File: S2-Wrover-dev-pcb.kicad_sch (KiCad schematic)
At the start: 23 parts, among them J1 USB_C_Receptacle_USB2.0, P1 CONN_02X13, P3 CONN_02X13, SW1 RESET, SW2 BOOT, U1 MCP1700-1202E_SOT23, U2 ESP32-S2-WROVER, U3 TPS2113APW, U4 TP4056

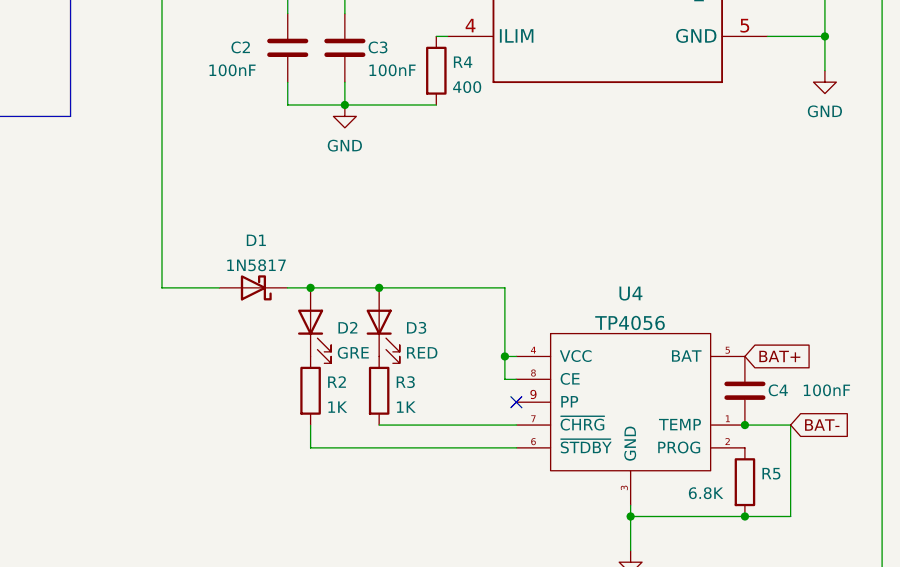
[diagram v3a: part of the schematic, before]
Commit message: Update schematic and assign footprints
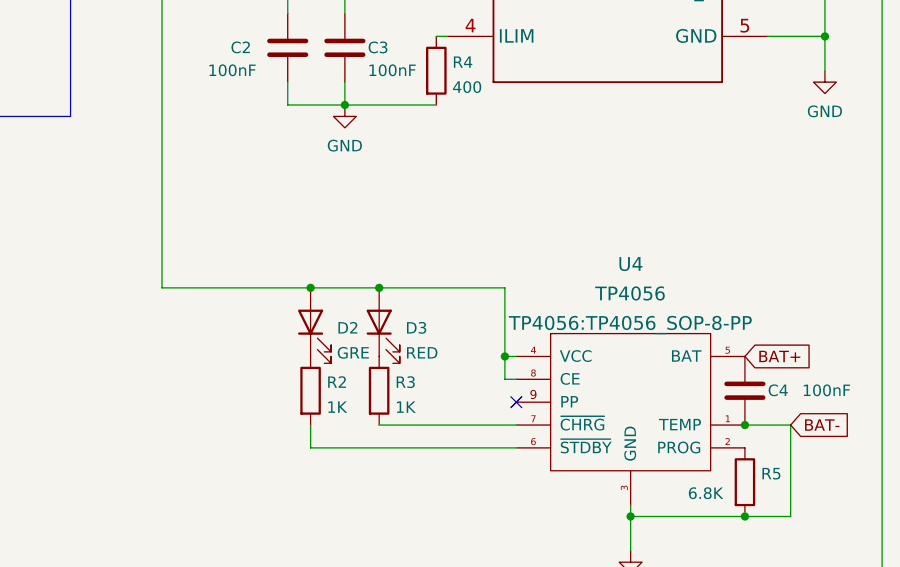
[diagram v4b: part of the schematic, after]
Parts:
- removed D1: 1N5817, Diode_SMD:D_SOD-123, symbol Device:D_Schottky
- P1, P3: footprint Pin_Headers:Pin_Header_Straight_2x13 -> Connector_PinHeader_2.54mm:PinHeader_2x13_P2.54mm_Vertical
- U3: footprint PW0008A_N -> footprint:TPS2113APW
- U4: footprint (none) -> TP4056:TP4056_SOP-8-PP
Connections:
- net VBUS: now also D2.2 (A), D3.2 (A), U4.4 (VCC), U4.8 (CE)
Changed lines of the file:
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@@
-    (stroke (width 0) (type default) (color 0 0 0 0))
-  )
-  (wire (pts (xy 213.36 86.36) (xy 215.9 86.36))
     (stroke (width 0) (type default) (color 0 0 0 0))
   )
@@
     (stroke (width 0) (type default) (color 0 0 0 0))
   )
-  (wire (pts (xy 199.39 86.36) (xy 205.74 86.36))
+  (wire (pts (xy 199.39 86.36) (xy 215.9 86.36))
     (stroke (width 0) (type default) (color 0 0 0 0))
   )
@@
     (property "Reference" "P1" (id 0) (at 125.73 146.05 0))
     (property "Value" "CONN_02X13" (id 1) (at 143.51 144.78 90))
-    (property "Footprint" "Pin_Headers:Pin_Header_Straight_2x13" (id 2) (at 172.72 146.05 0)
+    (property "Footprint" "Connector_PinHeader_2.54mm:PinHeader_2x13_P2.54mm_Vertical" (id 2) (at 172.72 146.05 0)
       (effects (font (size 1.27 1.27)) hide)
     )
@@
     (pin "9")
   )
-  (symbol (lib_id "Device:D_Schottky") (at 209.55 86.36 180) (unit 1)
-    (in_bom yes) (on_board yes) (fields_autoplaced)
-    (property "Reference" "D1" (id 0) (at 209.8675 81.1235 0))
-    (property "Value" "1N5817" (id 1) (at 209.8675 83.8986 0))
-    (property "Footprint" "Diode_SMD:D_SOD-123" (id 2) (at 209.55 86.36 0)
-      (effects (font (size 1.27 1.27)) hide)
-    )
-    (property "Datasheet" "~" (id 3) (at 209.55 86.36 0)
-      (effects (font (size 1.27 1.27)) hide)
-    )
-    (pin "1")
-    (pin "2")
-  )
   (symbol (lib_id "Device:LED") (at 223.52 90.17 90) (unit 1)
     (in_bom yes) (on_board yes) (fields_autoplaced)
@@
       (effects (font (size 1.524 1.524)))
     )
-    (property "Footprint" "PW0008A_N" (id 2) (at 248.92 52.324 0)
+    (property "Footprint" "footprint:TPS2113APW" (id 2) (at 248.92 52.324 0)
       (effects (font (size 1.524 1.524)) hide)
     )
@@
     (property "Reference" "P3" (id 0) (at 163.83 146.05 0))
     (property "Value" "CONN_02X13" (id 1) (at 181.61 144.78 90))
-    (property "Footprint" "Pin_Headers:Pin_Header_Straight_2x13" (id 2) (at 210.82 146.05 0)
+    (property "Footprint" "Connector_PinHeader_2.54mm:PinHeader_2x13_P2.54mm_Vertical" (id 2) (at 210.82 146.05 0)
       (effects (font (size 1.27 1.27)) hide)
     )
@@
   (symbol (lib_id "tp4056:TP4056") (at 251.46 100.33 0) (unit 1)
     (in_bom yes) (on_board yes) (fields_autoplaced)
-    (property "Reference" "U4" (id 0) (at 251.46 87.0361 0)
+    (property "Reference" "U4" (id 0) (at 251.46 83.7571 0)
       (effects (font (size 1.524 1.524)))
     )
-    (property "Value" "TP4056" (id 1) (at 251.46 90.3151 0)
+    (property "Value" "TP4056" (id 1) (at 251.46 87.0361 0)
       (effects (font (size 1.524 1.524)))
     )
-    (property "Footprint" "" (id 2) (at 251.46 100.33 0)
+    (property "Footprint" "TP4056:TP4056_SOP-8-PP" (id 2) (at 251.46 90.3151 0)
       (effects (font (size 1.524 1.524)))
     )
@@
       (reference "C4") (unit 1) (value "100nF") (footprint "Capacitor_SMD:C_0805_2012Metric")
     )
-    (path "/003cb78c-23ee-48ac-a35b-bde0860f178d"
-      (reference "D1") (unit 1) (value "1N5817") (footprint "Diode_SMD:D_SOD-123")
-    )
     (path "/e0ce6cb3-5c01-43ad-bab7-b796f3a1bb0f"
       (reference "D2") (unit 1) (value "GRE") (footprint "LED_SMD:LED_0805_2012Metric")
@@
     )
     (path "/00000000-0000-0000-0000-0000576c994f"
-      (reference "P1") (unit 1) (value "CONN_02X13") (footprint "Pin_Headers:Pin_Header_Straight_2x13")
+      (reference "P1") (unit 1) (value "CONN_02X13") (footprint "Connector_PinHeader_2.54mm:PinHeader_2x13_P2.54mm_Vertical")
     )
     (path "/9f932cfc-61d3-401a-b27a-c20d8327abe5"
-      (reference "P3") (unit 1) (value "CONN_02X13") (footprint "Pin_Headers:Pin_Header_Straight_2x13")
+      (reference "P3") (unit 1) (value "CONN_02X13") (footprint "Connector_PinHeader_2.54mm:PinHeader_2x13_P2.54mm_Vertical")
     )
     (path "/f7800b4d-8808-4d30-ba28-e36e5c5b35dc"
@@
     )
     (path "/38a48d5e-8f90-4cde-a529-54b3116299fc"
-      (reference "U3") (unit 1) (value "TPS2113APW") (footprint "PW0008A_N")
+      (reference "U3") (unit 1) (value "TPS2113APW") (footprint "footprint:TPS2113APW")
     )
     (path "/db763171-2d21-4254-a43f-5acafccd52ae"
-      (reference "U4") (unit 1) (value "TP4056") (footprint "")
-    )
-  )
+      (reference "U4") (unit 1) (value "TP4056") (footprint "TP4056:TP4056_SOP-8-PP")
+    )
+  )

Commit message: Update schematic
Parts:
- added J2: Jack-DC, Connector_JST:JST_EH_S2B-EH_1x02_P2.50mm_Horizontal, symbol Connector:Jack-DC
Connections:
- net BAT+: now also J2.2
- net GND: now also J2.1
- net VIN: now reaches U1.3 (VI), U3.7 (OUT)
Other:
- note added: "Battery jack"
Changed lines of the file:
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@@
+    (stroke (width 0) (type default) (color 0 0 0 0))
+  )
+  (polyline (pts (xy 153.67 77.47) (xy 153.67 80.01))
     (stroke (width 0) (type default) (color 0 0 0 0))
   )
@@
     (stroke (width 0) (type default) (color 0 0 0 0))
   )
-  (wire (pts (xy 78.74 127) (xy 78.74 106.68))
-    (stroke (width 0) (type default) (color 0 0 0 0))
-  )
   (wire (pts (xy 238.76 104.14) (xy 215.9 104.14))
     (stroke (width 0) (type default) (color 0 0 0 0))
@@
     (stroke (width 0) (type default) (color 0 0 0 0))
   )
+  (polyline (pts (xy 189.23 100.33) (xy 189.23 77.47))
+    (stroke (width 0) (type default) (color 0 0 0 0))
+  )
   (wire (pts (xy 172.72 41.91) (xy 172.72 53.34))
     (stroke (width 0) (type default) (color 0 0 0 0))
@@
     (stroke (width 0) (type default) (color 0 0 0 0))
   )
-  (wire (pts (xy 279.4 127) (xy 78.74 127))
-    (stroke (width 0) (type default) (color 0 0 0 0))
-  )
   (wire (pts (xy 181.61 135.89) (xy 181.61 138.43))
     (stroke (width 0) (type default) (color 0 0 0 0))
@@
     (stroke (width 0) (type default) (color 0 0 0 0))
   )
+  (polyline (pts (xy 189.23 77.47) (xy 153.67 77.47))
+    (stroke (width 0) (type default) (color 0 0 0 0))
+  )
   (wire (pts (xy 229.87 66.04) (xy 219.71 66.04))
     (stroke (width 0) (type default) (color 0 0 0 0))
@@
     (stroke (width 0) (type default) (color 0 0 0 0))
   )
-  (wire (pts (xy 279.4 43.18) (xy 279.4 127))
-    (stroke (width 0) (type default) (color 0 0 0 0))
-  )
   (wire (pts (xy 101.6 106.68) (xy 101.6 97.79))
     (stroke (width 0) (type default) (color 0 0 0 0))
@@
     (stroke (width 0) (type default) (color 0 0 0 0))
   )
+  (polyline (pts (xy 153.67 100.33) (xy 189.23 100.33))
+    (stroke (width 0) (type default) (color 0 0 0 0))
+  )
   (wire (pts (xy 215.9 86.36) (xy 223.52 86.36))
     (stroke (width 0) (type default) (color 0 0 0 0))
@@
     (stroke (width 0) (type default) (color 0 0 0 0))
   )
+  (wire (pts (xy 172.72 88.9) (xy 182.88 88.9))
+    (stroke (width 0) (type default) (color 0 0 0 0))
+  )
   (wire (pts (xy 194.31 135.89) (xy 194.31 138.43))
     (stroke (width 0) (type default) (color 0 0 0 0))
@@
     (stroke (width 0) (type default) (color 0 0 0 0))
   )
-  (wire (pts (xy 266.7 43.18) (xy 279.4 43.18))
-    (stroke (width 0) (type default) (color 0 0 0 0))
-  )
   (wire (pts (xy 158.75 135.89) (xy 158.75 138.43))
     (stroke (width 0) (type default) (color 0 0 0 0))
@@
     (stroke (width 0) (type default) (color 0 0 0 0))
   )
+  (polyline (pts (xy 153.67 80.01) (xy 153.67 100.33))
+    (stroke (width 0) (type default) (color 0 0 0 0))
+  )
   (wire (pts (xy 45.72 54.61) (xy 52.07 54.61))
     (stroke (width 0) (type default) (color 0 0 0 0))
@@
   )
   (text "Battery charging" (at 237.49 22.86 0)
+    (effects (font (size 1.27 1.27)) (justify left bottom))
+  )
+  (text "Battery jack" (at 156.21 74.93 0)
     (effects (font (size 1.27 1.27)) (justify left bottom))
   )
@@
     )
   )
+  (global_label "VIN" (shape input) (at 266.7 43.18 0) (fields_autoplaced)
+    (effects (font (size 1.27 1.27)) (justify left))
+    (property "Intersheet References" "${INTERSHEET_REFS}" (id 0) (at 272.3274 43.1006 0)
+      (effects (font (size 1.27 1.27)) (justify left) hide)
+    )
+  )
+  (global_label "BAT+" (shape input) (at 172.72 93.98 0) (fields_autoplaced)
+    (effects (font (size 1.27 1.27)) (justify left))
+    (property "Intersheet References" "${INTERSHEET_REFS}" (id 0) (at 180.2222 93.9006 0)
+      (effects (font (size 1.27 1.27)) (justify left) hide)
+    )
+  )
   (global_label "VBUS" (shape input) (at 48.26 36.83 0) (fields_autoplaced)
     (effects (font (size 1.27 1.27)) (justify left))
@@
     )
   )
-  (global_label "BAT-" (shape input) (at 269.24 101.6 0) (fields_autoplaced)
-    (effects (font (size 1.27 1.27)) (justify left))
-    (property "Intersheet References" "${INTERSHEET_REFS}" (id 0) (at 276.7422 101.5206 0)
-      (effects (font (size 1.27 1.27)) (justify left) hide)
+  (global_label "VIN" (shape input) (at 78.74 106.68 180) (fields_autoplaced)
+    (effects (font (size 1.27 1.27)) (justify right))
+    (property "Intersheet References" "${INTERSHEET_REFS}" (id 0) (at 73.1126 106.7594 0)
+      (effects (font (size 1.27 1.27)) (justify right) hide)
     )
   )
@@
     (pin "1")
     (pin "2")
+  )
+  (symbol (lib_id "Connector:Jack-DC") (at 165.1 91.44 0) (unit 1)
+    (in_bom yes) (on_board yes) (fields_autoplaced)
+    (property "Reference" "J2" (id 0) (at 165.1 83.6635 0))
+    (property "Value" "Jack-DC" (id 1) (at 165.1 86.4386 0))
+    (property "Footprint" "Connector_JST:JST_EH_S2B-EH_1x02_P2.50mm_Horizontal" (id 2) (at 166.37 92.456 0)
+      (effects (font (size 1.27 1.27)) hide)
+    )
+    (property "Datasheet" "~" (id 3) (at 166.37 92.456 0)
+      (effects (font (size 1.27 1.27)) hide)
+    )
+    (pin "1")
+    (pin "2")
+  )
+  (symbol (lib_id "power:GND") (at 182.88 88.9 0) (unit 1)
+    (in_bom yes) (on_board yes) (fields_autoplaced)
+    (property "Reference" "#PWR0102" (id 0) (at 182.88 95.25 0)
+      (effects (font (size 1.27 1.27)) hide)
+    )
+    (property "Value" "GND" (id 1) (at 182.88 93.4625 0))
+    (property "Footprint" "" (id 2) (at 182.88 88.9 0)
+      (effects (font (size 1.27 1.27)) hide)
+    )
+    (property "Datasheet" "" (id 3) (at 182.88 88.9 0)
+      (effects (font (size 1.27 1.27)) hide)
+    )
+    (pin "1")
   )
   (symbol (lib_id "power:GND") (at 172.72 55.88 0) (unit 1)
@@
       (reference "#PWR0101") (unit 1) (value "GND") (footprint "")
     )
+    (path "/566abc76-3191-496f-ae89-663e2ab9dd6d"
+      (reference "#PWR0102") (unit 1) (value "GND") (footprint "")
+    )
     (path "/64e8dbbe-977c-4d7f-a85e-1d328daab8b2"
       (reference "C1") (unit 1) (value "0.1u") (footprint "Capacitor_SMD:C_0805_2012Metric")
@@
       (reference "J1") (unit 1) (value "USB_C_Receptacle_USB2.0") (footprint "footprint:USB_C_Receptacle_HRO_TYPE-C-31-M-12")
     )
+    (path "/53179486-4fcd-487e-9d5f-27482ab43a55"
+      (reference "J2") (unit 1) (value "Jack-DC") (footprint "Connector_JST:JST_EH_S2B-EH_1x02_P2.50mm_Horizontal")
+    )
     (path "/00000000-0000-0000-0000-0000576c994f"

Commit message: V1 wiring
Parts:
- added C5: 0.1u, Capacitor_SMD:C_0805_2012Metric, symbol Device:C
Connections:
- net GND: now also C5.1
- net IO14: no longer P3.8 (Pin_8)
- net IO15: no longer P3.10 (Pin_10)
- net IO16: now also P3.8 (Pin_8); no longer P3.12 (Pin_12)
- net IO17: now also P3.10 (Pin_10); no longer P3.14 (Pin_14)
- net IO18: now also P3.12 (Pin_12)
- net IO21: now also P3.14 (Pin_14); no longer P3.16 (Pin_16)
- net IO33: now also P3.16 (Pin_16); no longer P3.18 (Pin_18)
- net IO34: now also P3.18 (Pin_18); no longer P3.20 (Pin_20)
- net IO35: now also P3.20 (Pin_20); no longer P3.22 (Pin_22)
- net IO36: now also P3.22 (Pin_22); no longer P3.24 (Pin_24)
- net IO37: now also P3.24 (Pin_24); no longer P3.26 (Pin_26)
- net at R1.2, SW1.1, U2.41 (EN): now also C5.2
- no-connect marks 17 -> 18
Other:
- moved on the sheet: R1
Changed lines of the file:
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@@
   (junction (at 264.16 101.6) (diameter 0) (color 0 0 0 0)
   )
+  (junction (at 129.54 92.71) (diameter 0) (color 0 0 0 0)
+  )
   (junction (at 160.02 41.91) (diameter 0) (color 0 0 0 0)
   )
+  (junction (at 123.19 92.71) (diameter 0) (color 0 0 0 0)
+  )
   (junction (at 48.26 49.53) (diameter 0) (color 0 0 0 0)
   )
@@
   (junction (at 264.16 111.76) (diameter 0) (color 0 0 0 0)
   )
+  (junction (at 140.97 92.71) (diameter 0) (color 0 0 0 0)
+  )
   (junction (at 237.49 93.98) (diameter 0) (color 0 0 0 0)
-  )
-  (junction (at 128.27 92.71) (diameter 0) (color 0 0 0 0)
   )
   (junction (at 120.65 132.08) (diameter 0) (color 0 0 0 0)
@@
   (no_connect (at 45.72 67.31))
   (no_connect (at 45.72 64.77))
+  (no_connect (at 196.85 135.89))
   (wire (pts (xy 101.6 35.56) (xy 101.6 39.37))
     (stroke (width 0) (type default) (color 0 0 0 0))
   )
-  (wire (pts (xy 128.27 106.68) (xy 101.6 106.68))
+  (wire (pts (xy 123.19 106.68) (xy 101.6 106.68))
     (stroke (width 0) (type default) (color 0 0 0 0))
   )
@@
     (stroke (width 0) (type default) (color 0 0 0 0))
   )
+  (wire (pts (xy 129.54 92.71) (xy 129.54 101.6))
+    (stroke (width 0) (type default) (color 0 0 0 0))
+  )
   (wire (pts (xy 83.82 57.15) (xy 86.36 57.15))
     (stroke (width 0) (type default) (color 0 0 0 0))
@@
     (stroke (width 0) (type default) (color 0 0 0 0))
   )
-  (wire (pts (xy 128.27 100.33) (xy 128.27 106.68))
+  (wire (pts (xy 123.19 100.33) (xy 123.19 106.68))
     (stroke (width 0) (type default) (color 0 0 0 0))
   )
@@
     (stroke (width 0) (type default) (color 0 0 0 0))
   )
+  (wire (pts (xy 129.54 101.6) (xy 139.7 101.6))
+    (stroke (width 0) (type default) (color 0 0 0 0))
+  )
   (wire (pts (xy 215.9 86.36) (xy 223.52 86.36))
     (stroke (width 0) (type default) (color 0 0 0 0))
@@
     (stroke (width 0) (type default) (color 0 0 0 0))
   )
+  (wire (pts (xy 140.97 92.71) (xy 144.78 92.71))
+    (stroke (width 0) (type default) (color 0 0 0 0))
+  )
   (wire (pts (xy 158.75 135.89) (xy 158.75 138.43))
     (stroke (width 0) (type default) (color 0 0 0 0))
@@
     (stroke (width 0) (type default) (color 0 0 0 0))
   )
-  (wire (pts (xy 130.81 92.71) (xy 128.27 92.71))
-    (stroke (width 0) (type default) (color 0 0 0 0))
-  )
   (wire (pts (xy 143.51 135.89) (xy 143.51 138.43))
     (stroke (width 0) (type default) (color 0 0 0 0))
@@
     (stroke (width 0) (type default) (color 0 0 0 0))
   )
+  (wire (pts (xy 129.54 92.71) (xy 130.81 92.71))
+    (stroke (width 0) (type default) (color 0 0 0 0))
+  )
   (wire (pts (xy 219.71 48.26) (xy 231.14 48.26))
     (stroke (width 0) (type default) (color 0 0 0 0))
@@
     (stroke (width 0) (type default) (color 0 0 0 0))
   )
+  (wire (pts (xy 123.19 92.71) (xy 129.54 92.71))
+    (stroke (width 0) (type default) (color 0 0 0 0))
+  )
   (wire (pts (xy 189.23 135.89) (xy 189.23 138.43))
     (stroke (width 0) (type default) (color 0 0 0 0))
@@
     (stroke (width 0) (type default) (color 0 0 0 0))
   )
-  (wire (pts (xy 116.84 92.71) (xy 128.27 92.71))
+  (wire (pts (xy 116.84 92.71) (xy 123.19 92.71))
     (stroke (width 0) (type default) (color 0 0 0 0))
   )
@@
     (stroke (width 0) (type default) (color 0 0 0 0))
   )
+  (wire (pts (xy 139.7 93.98) (xy 139.7 92.71))
+    (stroke (width 0) (type default) (color 0 0 0 0))
+  )
   (wire (pts (xy 179.07 135.89) (xy 179.07 138.43))
     (stroke (width 0) (type default) (color 0 0 0 0))
@@
     (stroke (width 0) (type default) (color 0 0 0 0))
   )
-  (wire (pts (xy 140.97 92.71) (xy 144.78 92.71))
+  (wire (pts (xy 139.7 92.71) (xy 140.97 92.71))
     (stroke (width 0) (type default) (color 0 0 0 0))
   )
@@
     (effects (font (size 1.27 1.27)) (justify left bottom))
   )
-  (label "IO36" (at 194.31 135.89 90)
-    (effects (font (size 1.27 1.27)) (justify left bottom))
-  )
-  (label "IO37" (at 196.85 135.89 90)
+  (label "IO37" (at 194.31 135.89 90)
     (effects (font (size 1.27 1.27)) (justify left bottom))
   )
@@
     (effects (font (size 1.27 1.27)) (justify left bottom))
   )
-  (label "IO14" (at 173.99 135.89 90)
-    (effects (font (size 1.27 1.27)) (justify left bottom))
-  )
-  (label "IO21" (at 184.15 135.89 90)
+  (label "IO16" (at 173.99 135.89 90)
+    (effects (font (size 1.27 1.27)) (justify left bottom))
+  )
+  (label "IO33" (at 184.15 135.89 90)
     (effects (font (size 1.27 1.27)) (justify left bottom))
   )
@@
     (effects (font (size 1.27 1.27)) (justify right bottom))
   )
-  (label "IO34" (at 189.23 135.89 90)
+  (label "IO35" (at 189.23 135.89 90)
     (effects (font (size 1.27 1.27)) (justify left bottom))
   )
@@
     (effects (font (size 1.27 1.27)) (justify right bottom))
   )
-  (label "IO33" (at 186.69 135.89 90)
+  (label "IO34" (at 186.69 135.89 90)
     (effects (font (size 1.27 1.27)) (justify left bottom))
   )
@@
     (effects (font (size 1.27 1.27)) (justify right bottom))
   )
-  (label "IO16" (at 179.07 135.89 90)
+  (label "IO18" (at 179.07 135.89 90)
     (effects (font (size 1.27 1.27)) (justify left bottom))
   )
@@
     (effects (font (size 1.27 1.27)) (justify right bottom))
   )
-  (label "IO17" (at 181.61 135.89 90)
+  (label "IO21" (at 181.61 135.89 90)
     (effects (font (size 1.27 1.27)) (justify left bottom))
   )
@@
     (effects (font (size 1.27 1.27)) (justify left bottom))
   )
-  (label "IO15" (at 176.53 135.89 90)
+  (label "IO17" (at 176.53 135.89 90)
     (effects (font (size 1.27 1.27)) (justify left bottom))
   )
@@
     (effects (font (size 1.27 1.27)) (justify left bottom))
   )
-  (label "IO35" (at 191.77 135.89 90)
+  (label "IO36" (at 191.77 135.89 90)
     (effects (font (size 1.27 1.27)) (justify left bottom))
   )
@@
     (pin "2")
   )
+  (symbol (lib_id "Device:C") (at 139.7 97.79 0) (unit 1)
+    (in_bom yes) (on_board yes)
+    (property "Reference" "C5" (id 0) (at 137.16 96.52 0)
+      (effects (font (size 1.27 1.27)) (justify right))
+    )
+    (property "Value" "0.1u" (id 1) (at 137.16 99.06 0)
+      (effects (font (size 1.27 1.27)) (justify right))
+    )
+    (property "Footprint" "Capacitor_SMD:C_0805_2012Metric" (id 2) (at 140.6652 101.6 0)
+      (effects (font (size 1.27 1.27)) hide)
+    )
+    (property "Datasheet" "~" (id 3) (at 139.7 97.79 0)
+      (effects (font (size 1.27 1.27)) hide)
+    )
+    (pin "1")
+    (pin "2")
+  )
   (symbol (lib_id "Device:R") (at 49.53 44.45 270) (unit 1)
     (in_bom yes) (on_board yes)
@@
     (pin "2")
   )
-  (symbol (lib_id "Device:R") (at 128.27 96.52 180) (unit 1)
-    (in_bom yes) (on_board yes) (fields_autoplaced)
-    (property "Reference" "R1" (id 0) (at 130.048 95.6115 0)
-      (effects (font (size 1.27 1.27)) (justify right))
-    )
-    (property "Value" "10K" (id 1) (at 130.048 98.3866 0)
-      (effects (font (size 1.27 1.27)) (justify right))
-    )
-    (property "Footprint" "Resistor_SMD:R_0603_1608Metric" (id 2) (at 130.048 96.52 90)
-      (effects (font (size 1.27 1.27)) hide)
-    )
-    (property "Datasheet" "~" (id 3) (at 128.27 96.52 0)
+  (symbol (lib_id "Device:R") (at 123.19 96.52 180) (unit 1)
+    (in_bom yes) (on_board yes) (fields_autoplaced)
+    (property "Reference" "R1" (id 0) (at 124.968 95.6115 0)
+      (effects (font (size 1.27 1.27)) (justify right))
+    )
+    (property "Value" "10K" (id 1) (at 124.968 98.3866 0)
+      (effects (font (size 1.27 1.27)) (justify right))
+    )
+    (property "Footprint" "Resistor_SMD:R_0603_1608Metric" (id 2) (at 124.968 96.52 90)
+      (effects (font (size 1.27 1.27)) hide)
+    )
+    (property "Datasheet" "~" (id 3) (at 123.19 96.52 0)
       (effects (font (size 1.27 1.27)) hide)
     )
@@
       (reference "C4") (unit 1) (value "100nF") (footprint "Capacitor_SMD:C_0805_2012Metric")
     )
+    (path "/ef5cc5e5-fd73-46e9-b81e-df62cf937821"
+      (reference "C5") (unit 1) (value "0.1u") (footprint "Capacitor_SMD:C_0805_2012Metric")
+    )
     (path "/e0ce6cb3-5c01-43ad-bab7-b796f3a1bb0f"
